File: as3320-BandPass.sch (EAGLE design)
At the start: 80 parts, among them IC1 CEM3320, IC2 TL074D, IC3 LM4040 5.0V, IC4 TL074D

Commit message: Updated to include FM in
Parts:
- added FM-LEVEL: 10kB, og-pots:POT_USVERTICAL
- added FM_IN: PJ301_THONKICONN6, og-pj301_variations:PJ301_THONKICONN6
- added IC5: TL072D, GMSN-R2Project:TL072D
- added R6: 100k, Pure VCF:GMSN_R-US_M0805
- added R8, R9: 62k, Pure VCF:GMSN_R-US_M0805
- renumbered R1-F2 to FREQUENCY, R55-RES2 to RESONANCE
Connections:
- new net N$1: IC5A.OUT, R6.2, R9.1
- new net N$2: IC5A.-IN, R6.1, R8.2
- new net N$7: FM-LEVEL.S, IC5A.+IN
- new net N$8: FM-LEVEL.E, FM_IN.3, R8.1
- net GND: now also FM-LEVEL.A, FM_IN.1, FM_IN.2
- net N$12: now also R9.2
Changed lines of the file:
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@@
 <setting verticaltext="up"/>
 </settings>
-<grid distance="0.1" unitdist="inch" unit="inch" style="lines" multiple="1" display="no" altdistance="0.01" altunitdist="inch" altunit="inch"/>
+<grid distance="0.1" unitdist="inch" unit="mm" style="lines" multiple="1" display="no" altdistance="0.01" altunitdist="inch" altunit="mm"/>
 <layers>
 <layer number="1" name="Top" color="4" fill="1" visible="no" active="no"/>
@@
 <part name="GND22" library="SparkFun" deviceset="GND" device=""/>
 <part name="C19" library="rcl" library_urn="urn:adsk.eagle:library:334" deviceset="C-US" device="C0805K" package3d_urn="urn:adsk.eagle:package:23681/2" value="300pF"/>
-<part name="R55-RES2" library="og-pots" deviceset="POT_US" device="VERTICAL" value="10kB"/>
+<part name="RESONANCE" library="og-pots" deviceset="POT_US" device="VERTICAL" value="10kB"/>
 <part name="GND27" library="SparkFun" deviceset="GND" device=""/>
 <part name="OUTPUT1" library="og-pj301_variations" deviceset="PJ301_THONKICONN" device="6"/>
@@
 <part name="V-OCT1" library="og-pj301_variations" deviceset="PJ301_THONKICONN" device="6"/>
 <part name="GND1" library="SparkFun" deviceset="GND" device=""/>
-<part name="R1-F2" library="og-pots" deviceset="POT_US" device="VERTICAL" value="10kB"/>
+<part name="FREQUENCY" library="og-pots" deviceset="POT_US" device="VERTICAL" value="10kB"/>
 <part name="R2" library="Pure VCF" deviceset="GMSN_R-US_" device="M0805" value="100k"/>
 <part name="R3" library="Pure VCF" deviceset="GMSN_R-US_" device="M0805" value="91k"/>
@@
 <part name="GND3" library="SparkFun" deviceset="GND" device=""/>
 <part name="OUTPUTLEVEL" library="GMSN" deviceset="9MMPOT" device="" value="100K"/>
+<part name="IC5" library="GMSN-R2Project" deviceset="TL072" device="D"/>
+<part name="R6" library="Pure VCF" deviceset="GMSN_R-US_" device="M0805" value="100k"/>
+<part name="R8" library="Pure VCF" deviceset="GMSN_R-US_" device="M0805" value="62k"/>
+<part name="R9" library="Pure VCF" deviceset="GMSN_R-US_" device="M0805" value="62k"/>
+<part name="FM-LEVEL" library="og-pots" deviceset="POT_US" device="VERTICAL" value="10kB"/>
+<part name="FM_IN" library="og-pj301_variations" deviceset="PJ301_THONKICONN" device="6"/>
+<part name="GND4" library="SparkFun" deviceset="GND" device=""/>
+<part name="GND6" library="SparkFun" deviceset="GND" device=""/>
 </parts>
 <sheets>
@@
 <attribute name="VALUE" x="-39.878" y="55.364" size="0.762" layer="96" font="vector" ratio="10" rot="R180" align="top-center"/>
 </instance>
-<instance part="R55-RES2" gate="G$1" x="-133.35" y="90.678" smashed="yes">
+<instance part="RESONANCE" gate="G$1" x="-133.35" y="90.678" smashed="yes">
 <attribute name="NAME" x="-138.43" y="88.138" size="1.778" layer="95" rot="R90"/>
 <attribute name="VALUE" x="-135.89" y="88.138" size="1.778" layer="96" rot="R90"/>
@@
 </segment>
 <segment>
-<pinref part="R55-RES2" gate="G$1" pin="A"/>
+<pinref part="RESONANCE" gate="G$1" pin="A"/>
 <pinref part="GND27" gate="1" pin="GND"/>
 <wire x1="-133.35" y1="83.058" x2="-133.35" y2="77.978" width="0.1524" layer="91"/>
@@
 </segment>
 <segment>
-<pinref part="R55-RES2" gate="G$1" pin="S"/>
+<pinref part="RESONANCE" gate="G$1" pin="S"/>
 <wire x1="-128.27" y1="90.678" x2="-123.19" y2="90.678" width="0.1524" layer="91"/>
 <label x="-123.19" y="90.678" size="1.778" layer="95"/>
@@
 <net name="RESONANCE_IN2" class="0">
 <segment>
-<pinref part="R55-RES2" gate="G$1" pin="E"/>
+<pinref part="RESONANCE" gate="G$1" pin="E"/>
 <wire x1="-133.35" y1="98.298" x2="-133.35" y2="110.998" width="0.1524" layer="91"/>
 <label x="-133.35" y="110.998" size="1.778" layer="95"/>
@@
 <attribute name="VALUE" x="81.28" y="17.78" size="1.778" layer="96" rot="MR0"/>
 </instance>
-<instance part="R1-F2" gate="G$1" x="71.12" y="53.34" smashed="yes">
+<instance part="FREQUENCY" gate="G$1" x="71.12" y="53.34" smashed="yes">
 <attribute name="NAME" x="66.04" y="50.8" size="1.778" layer="95" rot="R90"/>
 <attribute name="VALUE" x="68.58" y="50.8" size="1.778" layer="96" rot="R90"/>
@@
 <attribute name="NAME" x="132.08" y="59.055" size="1.778" layer="95"/>
 <attribute name="VALUE" x="132.08" y="50.8" size="1.778" layer="96"/>
+</instance>
+<instance part="IC5" gate="A" x="48.26" y="-5.08" smashed="yes">
+<attribute name="NAME" x="50.8" y="-8.255" size="1.778" layer="95" rot="MR180"/>
+<attribute name="VALUE" x="50.8" y="0" size="1.778" layer="96" rot="MR180"/>
+</instance>
+<instance part="R6" gate="G$1" x="45.72" y="10.16" smashed="yes">
+<attribute name="NAME" x="41.91" y="11.6586" size="1.778" layer="95"/>
+<attribute name="VALUE" x="41.91" y="6.858" size="1.778" layer="96"/>
+</instance>
+<instance part="R8" gate="G$1" x="30.48" y="-2.54" smashed="yes">
+<attribute name="NAME" x="26.67" y="-1.0414" size="1.778" layer="95"/>
+</instance>
+<instance part="R9" gate="G$1" x="68.58" y="-5.08" smashed="yes">
+<attribute name="NAME" x="64.77" y="-3.5814" size="1.778" layer="95"/>
+</instance>
+<instance part="FM-LEVEL" gate="G$1" x="15.24" y="-17.78" smashed="yes">
+<attribute name="NAME" x="10.16" y="-20.32" size="1.778" layer="95" rot="R90"/>
+<attribute name="VALUE" x="12.7" y="-20.32" size="1.778" layer="96" rot="R90"/>
+</instance>
+<instance part="FM_IN" gate="G$1" x="-10.16" y="-5.08" smashed="yes" rot="MR0">
+<attribute name="NAME" x="-7.62" y="-1.016" size="1.778" layer="95" rot="MR0"/>
+</instance>
+<instance part="GND4" gate="1" x="15.24" y="-33.02" smashed="yes" rot="MR0">
+<attribute name="VALUE" x="17.78" y="-35.56" size="1.778" layer="96" rot="MR0"/>
+</instance>
+<instance part="GND6" gate="1" x="0" y="-17.78" smashed="yes" rot="MR0">
+<attribute name="VALUE" x="2.54" y="-20.32" size="1.778" layer="96" rot="MR0"/>
 </instance>
 </instances>
@@
 </segment>
 <segment>
-<pinref part="R1-F2" gate="G$1" pin="A"/>
+<pinref part="FREQUENCY" gate="G$1" pin="A"/>
 <pinref part="GND31" gate="1" pin="GND"/>
 <wire x1="71.12" y1="45.72" x2="71.12" y2="43.18" width="0.1524" layer="91"/>
@@
 <label x="360.68" y="132.08" size="1.778" layer="95"/>
 </segment>
+<segment>
+<pinref part="FM_IN" gate="G$1" pin="2"/>
+<wire x1="-5.08" y1="-5.08" x2="0" y2="-5.08" width="0.1524" layer="91"/>
+<pinref part="GND6" gate="1" pin="GND"/>
+<wire x1="0" y1="-5.08" x2="0" y2="-7.62" width="0.1524" layer="91"/>
+<pinref part="FM_IN" gate="G$1" pin="1"/>
+<wire x1="0" y1="-7.62" x2="0" y2="-15.24" width="0.1524" layer="91"/>
+<wire x1="-5.08" y1="-7.62" x2="0" y2="-7.62" width="0.1524" layer="91"/>
+<junction x="0" y="-7.62"/>
+</segment>
+<segment>
+<pinref part="FM-LEVEL" gate="G$1" pin="A"/>
+<pinref part="GND4" gate="1" pin="GND"/>
+<wire x1="15.24" y1="-25.4" x2="15.24" y2="-30.48" width="0.1524" layer="91"/>
+</segment>
 </net>
 <net name="10V" class="1">
 <segment>
-<pinref part="R1-F2" gate="G$1" pin="E"/>
+<pinref part="FREQUENCY" gate="G$1" pin="E"/>
 <wire x1="71.12" y1="60.96" x2="71.12" y2="68.58" width="0.1524" layer="91"/>
 <wire x1="71.12" y1="68.58" x2="53.34" y2="68.58" width="0.1524" layer="91"/>
@@
 <net name="N$5" class="0">
 <segment>
-<pinref part="R1-F2" gate="G$1" pin="S"/>
+<pinref part="FREQUENCY" gate="G$1" pin="S"/>
 <pinref part="R2" gate="G$1" pin="1"/>
 <wire x1="76.2" y1="53.34" x2="86.36" y2="53.34" width="0.1524" layer="91"/>
@@
 <junction x="99.06" y="30.48"/>
 <pinref part="IC2" gate="D" pin="+IN"/>
+<wire x1="99.06" y1="7.62" x2="99.06" y2="-5.08" width="0.1524" layer="91"/>
+<junction x="99.06" y="7.62"/>
+<pinref part="R9" gate="G$1" pin="2"/>
+<wire x1="99.06" y1="-5.08" x2="73.66" y2="-5.08" width="0.1524" layer="91"/>
 </segment>
 </net>
@@
 </segment>
 </net>
+<net name="N$1" class="0">
+<segment>
+<pinref part="R9" gate="G$1" pin="1"/>
+<pinref part="IC5" gate="A" pin="OUT"/>
+<wire x1="63.5" y1="-5.08" x2="55.88" y2="-5.08" width="0.1524" layer="91"/>
+<wire x1="55.88" y1="-5.08" x2="55.88" y2="10.16" width="0.1524" layer="91"/>
+<junction x="55.88" y="-5.08"/>
+<pinref part="R6" gate="G$1" pin="2"/>
+<wire x1="55.88" y1="10.16" x2="50.8" y2="10.16" width="0.1524" layer="91"/>
+</segment>
+</net>
+<net name="N$2" class="0">
+<segment>
+<pinref part="R6" gate="G$1" pin="1"/>
+<wire x1="40.64" y1="10.16" x2="35.56" y2="10.16" width="0.1524" layer="91"/>
+<pinref part="R8" gate="G$1" pin="2"/>
+<wire x1="35.56" y1="10.16" x2="35.56" y2="-2.54" width="0.1524" layer="91"/>
+<pinref part="IC5" gate="A" pin="-IN"/>
+<wire x1="35.56" y1="-2.54" x2="40.64" y2="-2.54" width="0.1524" layer="91"/>
+<junction x="35.56" y="-2.54"/>
+</segment>
+</net>
+<net name="N$7" class="0">
+<segment>
+<pinref part="FM-LEVEL" gate="G$1" pin="S"/>
+<wire x1="20.32" y1="-17.78" x2="35.56" y2="-17.78" width="0.1524" layer="91"/>
+<wire x1="35.56" y1="-17.78" x2="35.56" y2="-7.62" width="0.1524" layer="91"/>
+<pinref part="IC5" gate="A" pin="+IN"/>
+<wire x1="35.56" y1="-7.62" x2="40.64" y2="-7.62" width="0.1524" layer="91"/>
+</segment>
+</net>
+<net name="N$8" class="0">
+<segment>
+<pinref part="FM_IN" gate="G$1" pin="3"/>
+<pinref part="R8" gate="G$1" pin="1"/>
+<wire x1="-5.08" y1="-2.54" x2="15.24" y2="-2.54" width="0.1524" layer="91"/>
+<pinref part="FM-LEVEL" gate="G$1" pin="E"/>
+<wire x1="15.24" y1="-2.54" x2="25.4" y2="-2.54" width="0.1524" layer="91"/>
+<wire x1="15.24" y1="-10.16" x2="15.24" y2="-2.54" width="0.1524" layer="91"/>
+<junction x="15.24" y="-2.54"/>
+</segment>
+</net>

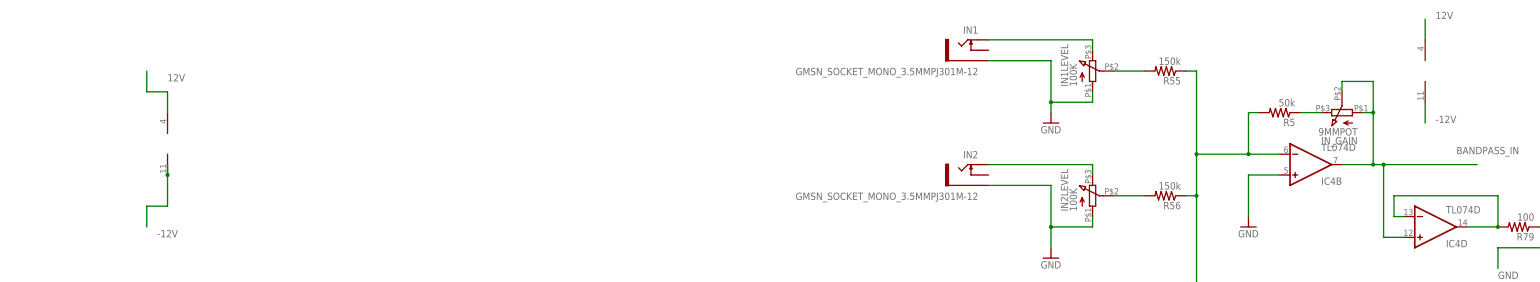
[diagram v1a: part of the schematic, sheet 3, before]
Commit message: added power for IC5
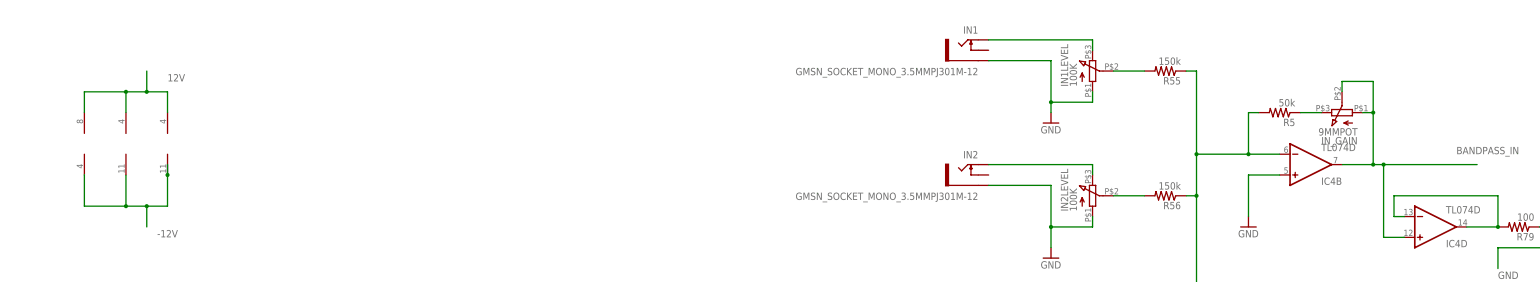
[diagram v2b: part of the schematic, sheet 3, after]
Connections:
- net -12V: now also IC5P.V-
- net 12V: now also IC5P.V+
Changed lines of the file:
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@@
 <setting verticaltext="up"/>
 </settings>
-<grid distance="0.1" unitdist="inch" unit="mm" style="lines" multiple="1" display="no" altdistance="0.01" altunitdist="inch" altunit="mm"/>
+<grid distance="0.1" unitdist="inch" unit="inch" style="lines" multiple="1" display="no" altdistance="0.01" altunitdist="inch" altunit="inch"/>
 <layers>
 <layer number="1" name="Top" color="4" fill="1" visible="no" active="no"/>
@@
 <attribute name="VALUE" x="283.21" y="122.682" size="1.778" layer="96" rot="R180"/>
 </instance>
-<instance part="IC4" gate="P" x="342.9" y="182.88" smashed="yes"/>
+<instance part="IC4" gate="P" x="25.4" y="165.1" smashed="yes"/>
 <instance part="RES-2" gate="G$1" x="228.6" y="10.16" smashed="yes" rot="MR0">
 <attribute name="NAME" x="231.14" y="14.224" size="1.778" layer="95" rot="MR0"/>
@@
 <attribute name="VALUE" x="2.54" y="-20.32" size="1.778" layer="96" rot="MR0"/>
 </instance>
+<instance part="IC5" gate="P" x="15.24" y="165.1" smashed="yes"/>
 </instances>
 <busses>
@@
 <wire x1="30.48" y1="177.8" x2="30.48" y2="182.88" width="0.1524" layer="91"/>
 <label x="35.56" y="180.34" size="1.778" layer="95"/>
-</segment>
-<segment>
 <pinref part="IC4" gate="P" pin="V+"/>
-<wire x1="342.9" y1="190.5" x2="342.9" y2="195.58" width="0.1524" layer="91"/>
-<label x="345.44" y="195.58" size="1.778" layer="95"/>
+<wire x1="25.4" y1="172.72" x2="25.4" y2="177.8" width="0.1524" layer="91"/>
+<wire x1="25.4" y1="177.8" x2="30.48" y2="177.8" width="0.1524" layer="91"/>
+<junction x="30.48" y="177.8"/>
+<pinref part="IC5" gate="P" pin="V+"/>
+<wire x1="15.24" y1="172.72" x2="15.24" y2="177.8" width="0.1524" layer="91"/>
+<wire x1="15.24" y1="177.8" x2="25.4" y2="177.8" width="0.1524" layer="91"/>
+<junction x="25.4" y="177.8"/>
 </segment>
 </net>
@@
 <wire x1="30.48" y1="149.86" x2="30.48" y2="144.78" width="0.1524" layer="91"/>
 <label x="33.02" y="142.24" size="1.778" layer="95"/>
-</segment>
-<segment>
 <pinref part="IC4" gate="P" pin="V-"/>
-<wire x1="342.9" y1="175.26" x2="342.9" y2="170.18" width="0.1524" layer="91"/>
-<label x="345.44" y="170.18" size="1.778" layer="95"/>
-</segment>
-</net>
+<wire x1="25.4" y1="157.48" x2="25.4" y2="149.86" width="0.1524" layer="91"/>
+<wire x1="25.4" y1="149.86" x2="30.48" y2="149.86" width="0.1524" layer="91"/>
+<junction x="30.48" y="149.86"/>
+<pinref part="IC5" gate="P" pin="V-"/>
+<wire x1="15.24" y1="157.48" x2="15.24" y2="149.86" width="0.1524" layer="91"/>
+<wire x1="15.24" y1="149.86" x2="25.4" y2="149.86" width="0.1524" layer="91"/>
+<junction x="25.4" y="149.86"/>
+</segment>
+</net>
